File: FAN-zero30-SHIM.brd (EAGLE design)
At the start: 38.3 x 65 mm, 10 parts

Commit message: Connecting dots.
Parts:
- moved SJ2 0.38 mm to (10.9, 3.43)
- moved SJ3 0.25 mm to (19.1, 3.43)
- turned SJ1 to 270 degrees
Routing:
- net VFAN: track 0.00 -> 55.2 mm, vias 0 -> 1
- net GPIO4: track 0.00 -> 54.0 mm, vias 0 -> 2
- net 3.3V: track 0.00 -> 45.3 mm
- net 5V: track 0.00 -> 28.6 mm
- net PWM: track 0.00 -> 21.0 mm, vias 0 -> 1
- net GPIO16: track 0.00 -> 20.1 mm, vias 0 -> 2
- net GPIO12: track 0.00 -> 19.4 mm, vias 0 -> 1
- net GPIO13: track 0.00 -> 16.2 mm, vias 0 -> 1
- net TACH: track 0.00 -> 11.2 mm, vias 0 -> 1
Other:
- board text added: "3.3V"
- board text added: "5V"
- board text added: "FAN-zero30-SHIM v1.0"
- board text added: "Fan PWM"
- board text added: "Fan tacho"
- board text added: "Fan voltage"
- board text added: "IO12"
- board text added: "IO13"
- board text added: "IO16"
- board text added: "IO4"
- board text removed: "FAN-zero-SHIM v1.0"

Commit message: Connecting dots.
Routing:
- net GPIO12: track 19.4 -> 20.1 mm
- net GPIO13: track 16.2 -> 17.0 mm
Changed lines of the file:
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@@
 <via x="11.303" y="6.858" extent="1-16" drill="0.35"/>
 <via x="15.4432" y="6.1976" extent="1-16" drill="0.35"/>
-<via x="18.161" y="8.255" extent="1-16" drill="0.35"/>
-<via x="21.336" y="9.652" extent="1-16" drill="0.35"/>
+<via x="18.288" y="8.89" extent="1-16" drill="0.35"/>
+<via x="21.082" y="9.906" extent="1-16" drill="0.35"/>
 <via x="10.033" y="9.652" extent="1-16" drill="0.35"/>
 <via x="14.859" y="10.033" extent="1-16" drill="0.35"/>
@@
 <via x="22.733" y="26.289" extent="1-16" drill="0.35"/>
 <via x="22.479" y="17.145" extent="1-16" drill="0.35"/>
-<via x="20.701" y="13.0302" extent="1-16" drill="0.35"/>
 <via x="18.923" y="13.589" extent="1-16" drill="0.35"/>
 <via x="-5.588" y="26.797" extent="1-16" drill="0.35"/>
@@
 <via x="8.1534" y="12.1666" extent="1-16" drill="0.35"/>
 <via x="15.24" y="0.762" extent="1-16" drill="0.35"/>
-<via x="23.5966" y="12.9286" extent="1-16" drill="0.35"/>
-<via x="23.749" y="11.303" extent="1-16" drill="0.35"/>
-<via x="23.5204" y="15.8496" extent="1-16" drill="0.35"/>
+<via x="23.2156" y="13.4366" extent="1-16" drill="0.35"/>
+<via x="23.241" y="11.176" extent="1-16" drill="0.35"/>
 <via x="14.6812" y="58.2168" extent="1-16" drill="0.35"/>
 <via x="14.7066" y="54.61" extent="1-16" drill="0.35"/>
@@
 <via x="1.1176" y="52.2986" extent="1-16" drill="0.35"/>
 <via x="19.3802" y="5.4102" extent="1-16" drill="0.35"/>
-<via x="21.1582" y="5.5372" extent="1-16" drill="0.35"/>
+<via x="21.6662" y="5.1562" extent="1-16" drill="0.35"/>
 </signal>
 <signal name="3.3V">
@@
 <wire x1="23.1982" y1="47.117" x2="22.86" y2="47.117" width="0.254" layer="1"/>
 <via x="22.86" y="47.117" extent="1-16" drill="0.35"/>
-<wire x1="22.86" y1="47.117" x2="22.987" y2="46.99" width="0.254" layer="16"/>
-<wire x1="22.987" y1="46.99" x2="22.987" y2="37.79223125" width="0.254" layer="16"/>
-<wire x1="22.987" y1="37.79223125" x2="23.603" y2="37.17623125" width="0.254" layer="16"/>
+<wire x1="22.86" y1="47.117" x2="22.86" y2="37.66523125" width="0.254" layer="16"/>
+<wire x1="22.86" y1="37.66523125" x2="23.603" y2="36.92223125" width="0.254" layer="16"/>
 <via x="9.779" y="4.826" extent="1-16" drill="0.35"/>
-<wire x1="23.603" y1="37.17623125" x2="23.603" y2="17.0088125" width="0.254" layer="16"/>
+<wire x1="23.603" y1="36.92223125" x2="23.603" y2="17.0088125" width="0.254" layer="16"/>
 <wire x1="11.2705875" y1="4.6764" x2="10.1416125" y2="4.6764" width="0.254" layer="16"/>
 <wire x1="10.1416125" y1="4.6764" x2="9.9920125" y2="4.826" width="0.254" layer="16"/>
@@
 <contactref element="J3" pad="17"/>
 <contactref element="SJ3" pad="3"/>
-<wire x1="25.4318" y1="15.975" x2="24.746" y2="15.975" width="0.254" layer="16"/>
-<wire x1="24.746" y1="15.975" x2="19.558" y2="10.787" width="0.254" layer="16"/>
-<wire x1="19.558" y1="10.787" x2="19.558" y2="6.6294" width="0.254" layer="16"/>
+<wire x1="25.4318" y1="15.975" x2="24.9238" y2="15.467" width="0.254" layer="16"/>
+<wire x1="24.9238" y1="15.467" x2="22.968" y2="15.467" width="0.254" layer="16"/>
+<wire x1="22.968" y1="15.467" x2="19.558" y2="12.057" width="0.254" layer="16"/>
+<wire x1="19.558" y1="12.057" x2="19.558" y2="6.6294" width="0.254" layer="16"/>
 <wire x1="19.558" y1="6.6294" x2="17.907" y2="4.9784" width="0.254" layer="16"/>
 <wire x1="17.907" y1="4.9784" x2="17.907" y2="4.826" width="0.254" layer="16"/>
@@
 <wire x1="27.6162" y1="17.4736" x2="26.7018" y2="16.5592" width="0.254" layer="16"/>
 <wire x1="26.7018" y1="16.5592" x2="26.7018" y2="15.2667875" width="0.254" layer="16"/>
-<wire x1="26.1908125" y1="14.7558" x2="24.4187875" y2="14.7558" width="0.254" layer="16"/>
-<wire x1="24.4187875" y1="14.7558" x2="20.193" y2="10.5300125" width="0.254" layer="16"/>
-<wire x1="20.193" y1="10.5300125" x2="20.193" y2="4.826" width="0.254" layer="16"/>
+<wire x1="26.1908125" y1="14.7558" x2="23.1487875" y2="14.7558" width="0.254" layer="16"/>
+<wire x1="23.1487875" y1="14.7558" x2="20.193" y2="11.8000125" width="0.254" layer="16"/>
+<wire x1="20.193" y1="11.8000125" x2="20.193" y2="4.826" width="0.254" layer="16"/>
 <wire x1="20.193" y1="4.826" x2="20.193" y2="3.81" width="0.254" layer="1"/>
 <wire x1="20.193" y1="3.81" x2="20.574" y2="3.429" width="0.254" layer="1"/>
@@
 <contactref element="J4" pad="18"/>
 <contactref element="SJ2" pad="1"/>
-<wire x1="27.6162" y1="13.435" x2="26.3576125" y2="12.1764125" width="0.254" layer="1"/>
-<wire x1="26.3576125" y1="12.1764125" x2="19.8783875" y2="12.1764125" width="0.254" layer="1"/>
-<via x="19.8783875" y="12.1764125" extent="1-16" drill="0.35"/>
-<wire x1="19.8783875" y1="12.1764125" x2="12.527975" y2="4.826" width="0.254" layer="16"/>
-<wire x1="12.446" y1="4.826" x2="12.527975" y2="4.826" width="0.254" layer="16"/>
+<wire x1="27.6162" y1="13.435" x2="26.9812" y2="13.435" width="0.254" layer="1"/>
+<wire x1="26.9812" y1="13.435" x2="25.7112" y2="12.165" width="0.254" layer="1"/>
+<wire x1="25.7112" y1="12.165" x2="19.739975" y2="12.165" width="0.254" layer="1"/>
+<wire x1="19.739975" y1="12.165" x2="18.8623875" y2="11.2874125" width="0.254" layer="1"/>
+<via x="18.8623875" y="11.2874125" extent="1-16" drill="0.35"/>
+<wire x1="18.8623875" y1="11.2874125" x2="12.446" y2="4.871025" width="0.254" layer="16"/>
+<wire x1="12.446" y1="4.826" x2="12.446" y2="4.871025" width="0.254" layer="16"/>
 <via x="12.446" y="4.826" extent="1-16" drill="0.35"/>
 <wire x1="12.446" y1="4.826" x2="12.446" y2="3.429" width="0.254" layer="1"/>

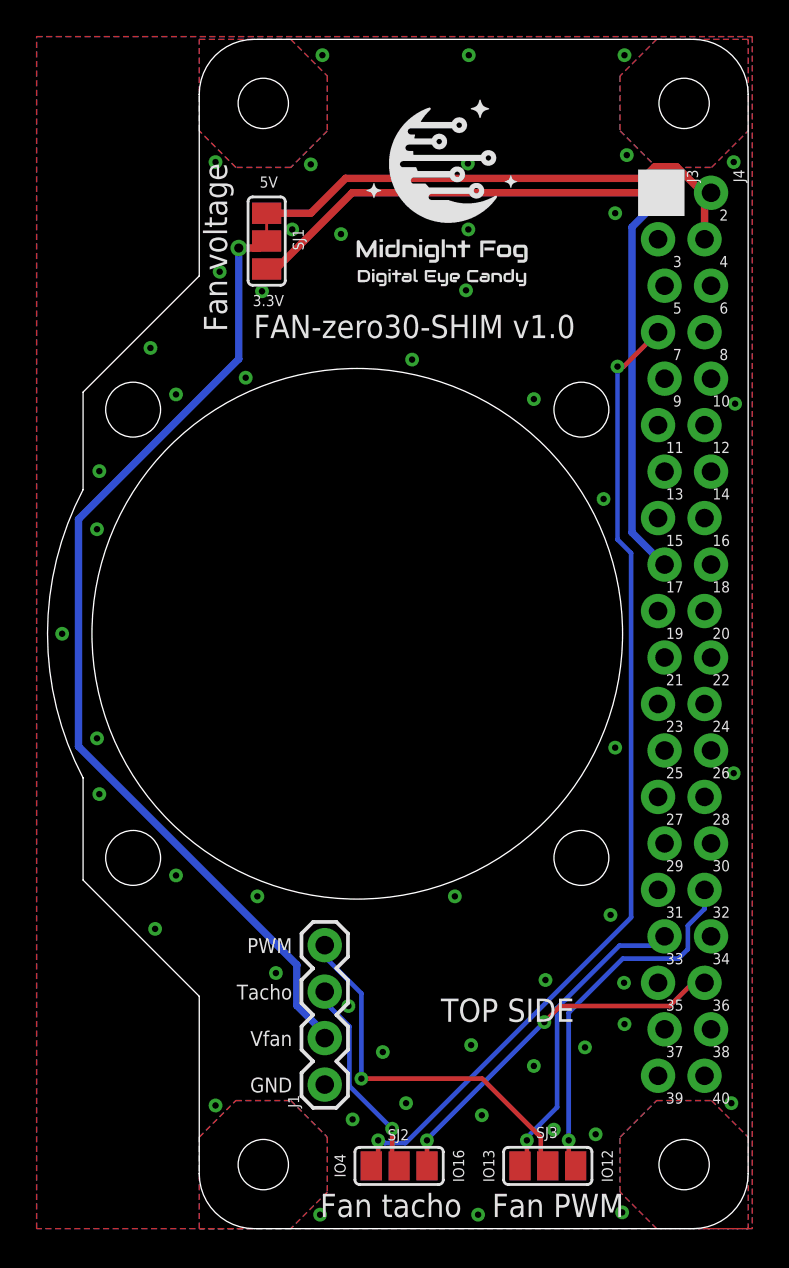
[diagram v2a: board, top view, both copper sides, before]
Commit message: Moved some traces around.
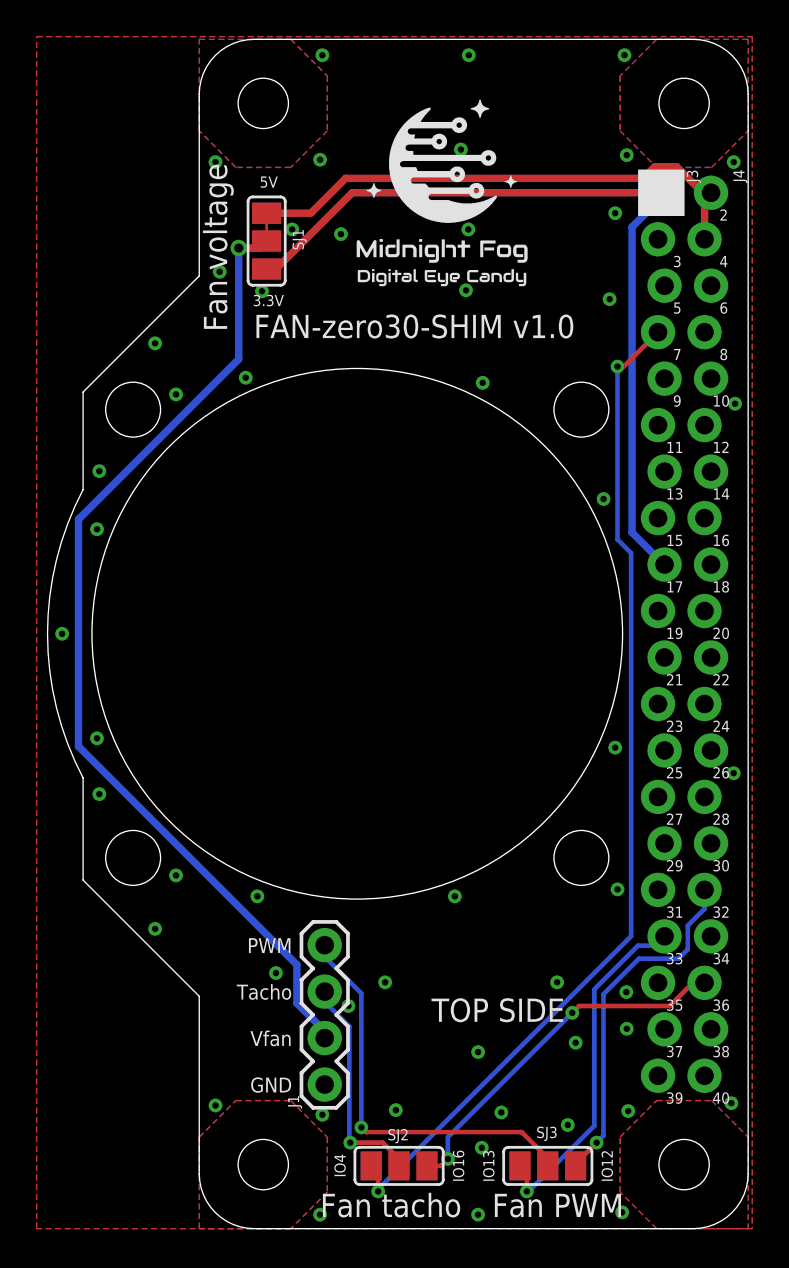
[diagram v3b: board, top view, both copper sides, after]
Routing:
- net GPIO13: track 17.0 -> 19.2 mm
- net GPIO4: track 54.0 -> 55.7 mm
- net PWM: track 21.0 -> 22.1 mm
- net TACH: track 11.2 -> 12.2 mm
- net GPIO12: track 20.1 -> 19.3 mm
